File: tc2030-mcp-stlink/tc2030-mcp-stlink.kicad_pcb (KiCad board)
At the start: 2 copper layers, 30.5 x 30.7 mm, 3 parts, among them J2 SFH11-PBPC-D10-ST-BK, J3 5555165-1

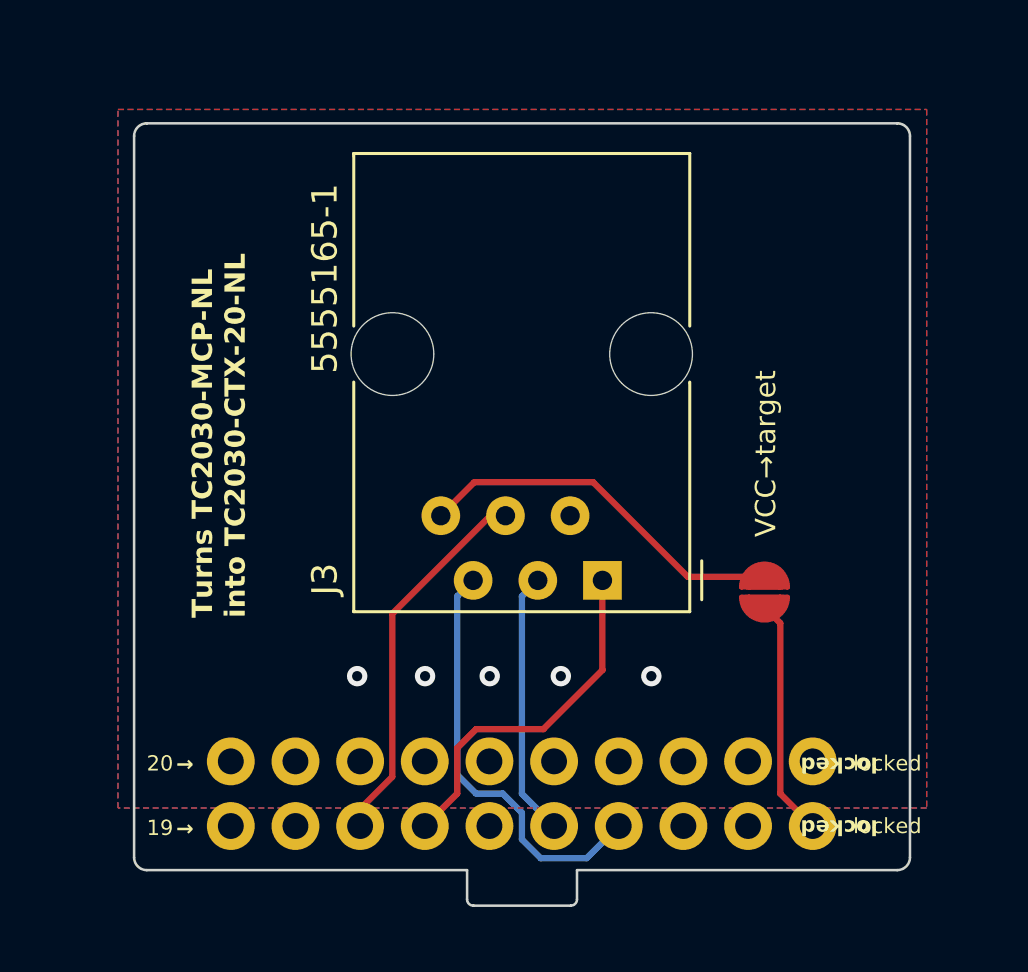
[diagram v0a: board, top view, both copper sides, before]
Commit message: flipped st-link pinout
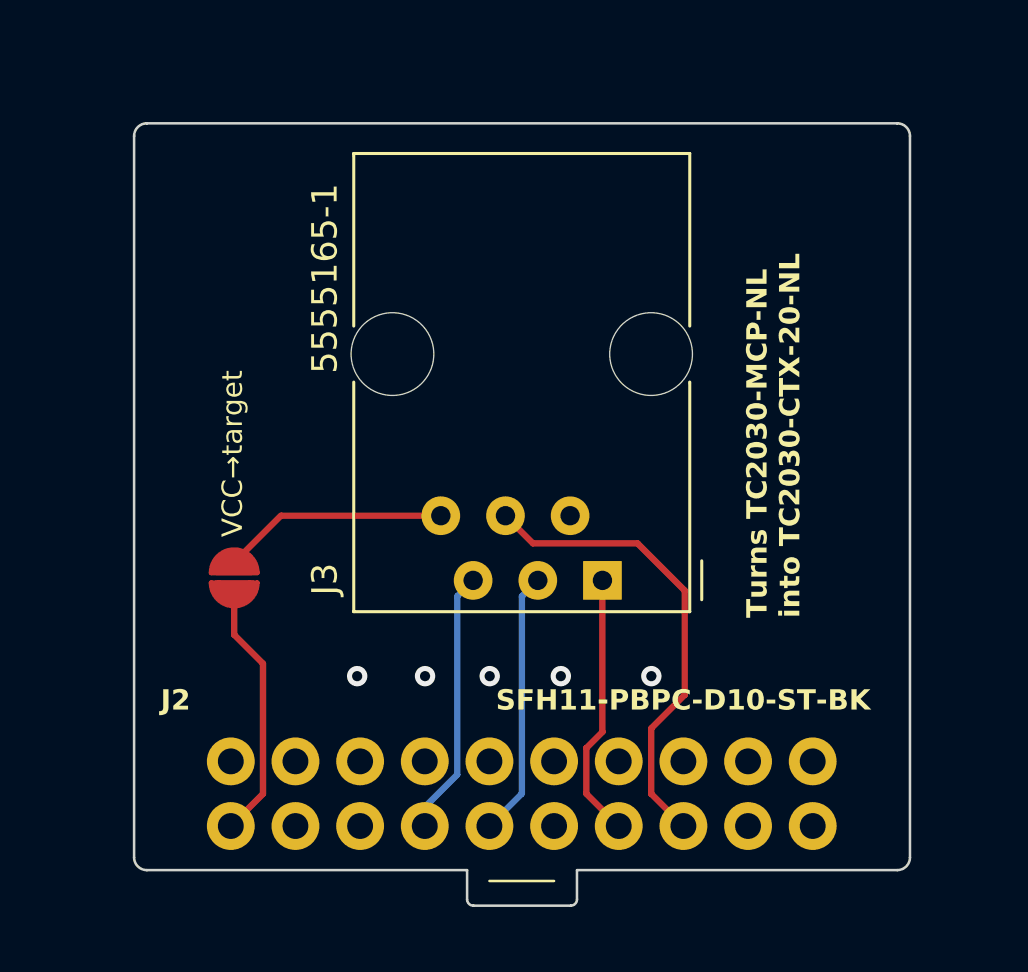
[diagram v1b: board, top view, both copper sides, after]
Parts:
- J2: moved to F.Cu
- moved JP1 20.8 mm to (14.6, -3.10)
- turned J2 to 0 degrees
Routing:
- net SWDIO: track 16.7 -> 10.4 mm
- net VCC: track 14.8 -> 8.88 mm
- net NRST: track 14.9 -> 18.6 mm
- net SWO: track 14.1 -> 10.4 mm
- net Net-(J2-VTREF): track 9.37 -> 10.1 mm
- removed copper zone on B.Cu, net GND
- removed copper zone on F.Cu, net GND
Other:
- board text removed: "locked"
- board text removed: "→"

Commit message: fix stlink pinout
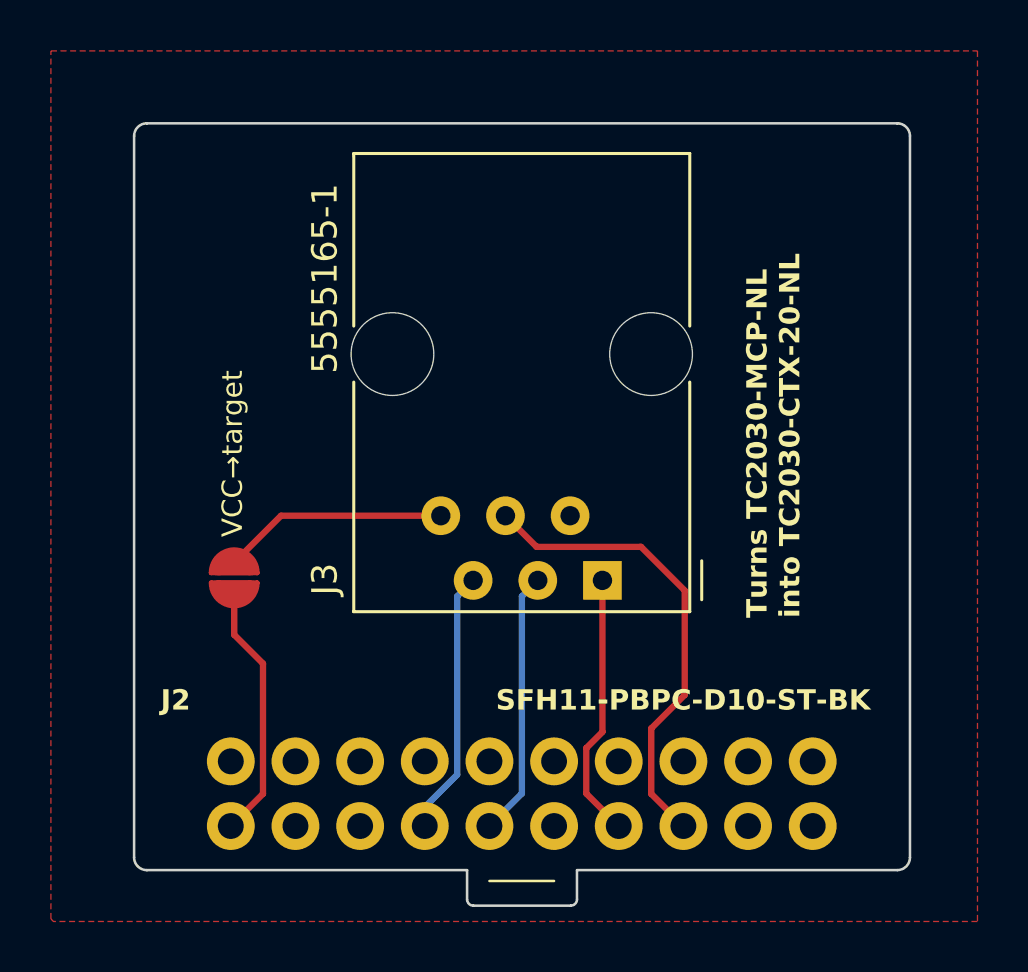
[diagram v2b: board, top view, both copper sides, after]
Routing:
- net GND: vias 5 -> 0
- added copper zone on F.Cu, net GND
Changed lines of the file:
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@@
     (effects (font (size 0.8 0.8) (thickness 0.15)) (justify left bottom))
   )
-  (via (at 22.098 0.762) (size 0.8) (drill 0.4) (layers "F.Cu" "B.Cu") (free) (net 1))
-  (via (at 19.431 0.762) (size 0.8) (drill 0.4) (layers "F.Cu" "B.Cu") (free) (net 1))
-  (via (at 30.988 0.762) (size 0.8) (drill 0.4) (layers "F.Cu" "B.Cu") (free) (net 1))
-  (via (at 27.432 0.762) (size 0.8) (drill 0.4) (layers "F.Cu" "B.Cu") (free) (net 1))
-  (via (at 24.638 0.762) (size 0.8) (drill 0.4) (layers "F.Cu" "B.Cu") (free) (net 1))
   (segment (start 14.6 -3.7) (end 16.44 -5.54) (width 0.25) (layer "F.Cu") (net 8))
   (segment (start 16.44 -5.54) (end 22.717142 -5.54) (width 0.25) (layer "F.Cu") (net 8))
@@
   (segment (start 22.087142 6.65) (end 22.087142 5.909098) (width 0.25) (layer "B.Cu") (net 9))
   (segment (start 23.362342 -2.3752) (end 23.987142 -3) (width 0.25) (layer "B.Cu") (net 9))
+  (segment (start 26.479142 -4.318) (end 25.257142 -5.54) (width 0.25) (layer "F.Cu") (net 10))
+  (segment (start 30.982342 5.3852) (end 30.982342 2.817658) (width 0.25) (layer "F.Cu") (net 10))
+  (segment (start 32.3 -2.6) (end 30.582 -4.318) (width 0.25) (layer "F.Cu") (net 10))
+  (segment (start 32.247142 6.65) (end 30.982342 5.3852) (width 0.25) (layer "F.Cu") (net 10))
+  (segment (start 30.582 -4.318) (end 26.479142 -4.318) (width 0.25) (layer "F.Cu") (net 10))
   (segment (start 30.982342 2.817658) (end 32.3 1.5) (width 0.25) (layer "F.Cu") (net 10))
   (segment (start 32.3 1.5) (end 32.3 -2.6) (width 0.25) (layer "F.Cu") (net 10))
-  (segment (start 30.982342 5.3852) (end 30.982342 2.817658) (width 0.25) (layer "F.Cu") (net 10))
-  (segment (start 26.342142 -4.455) (end 25.257142 -5.54) (width 0.25) (layer "F.Cu") (net 10))
-  (segment (start 30.445 -4.455) (end 26.342142 -4.455) (width 0.25) (layer "F.Cu") (net 10))
-  (segment (start 32.3 -2.6) (end 30.445 -4.455) (width 0.25) (layer "F.Cu") (net 10))
-  (segment (start 32.247142 6.65) (end 30.982342 5.3852) (width 0.25) (layer "F.Cu") (net 10))
   (segment (start 24.627142 6.65) (end 25.902342 5.3748) (width 0.25) (layer "B.Cu") (net 11))
   (segment (start 25.902342 -2.3752) (end 26.527142 -3) (width 0.25) (layer "B.Cu") (net 11))
@@
   (segment (start 15.731942 0.268058) (end 15.731942 5.3852) (width 0.25) (layer "F.Cu") (net 13))
   (segment (start 15.731942 5.3852) (end 14.467142 6.65) (width 0.25) (layer "F.Cu") (net 13))
+  (zone (net 1) (net_name "GND") (layer "F.Cu") (hatch edge 0.5)
+    (connect_pads (clearance 0.5))
+    (min_thickness 0.25) (filled_areas_thickness no)
+    (fill yes (thermal_gap 0.5) (thermal_bridge_width 0.5))
+    (polygon
+      (pts
+        (xy 7.4 -23.8)
+        (xy 43.8 -23.8)
+        (xy 43.8 10.4)
+        (xy 7.5 10.4)
+        (xy 7.4 10.3)
+      )
+    )
+  )
 )
